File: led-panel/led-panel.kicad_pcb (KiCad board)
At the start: 2 copper layers, 129 parts, among them J1 Conn_01x24

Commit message: routing done
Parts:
- moved J1 2.62 mm to (106.7, 108.0)
- moved D100 1.80 mm to (167.6, 83.8)
- moved D106 1.80 mm to (172.7, 73.7)
- moved D107 1.80 mm to (172.7, 78.7)
- moved D108 1.80 mm to (172.7, 83.8)
- moved D122 1.80 mm to (182.9, 73.7)
- moved D123 1.80 mm to (182.9, 78.7)
- moved D124 1.80 mm to (182.9, 83.8)
- moved D34 1.80 mm to (127.0, 73.7)
- moved D35 1.80 mm to (127.0, 78.7)
- moved D36 1.80 mm to (127.0, 83.8)
- moved D50 1.80 mm to (137.2, 73.7)
- moved D51 1.80 mm to (137.2, 78.7)
- moved D52 1.80 mm to (137.2, 83.8)
- moved D66 1.80 mm to (147.3, 73.7)
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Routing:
- net Net-(D0-Pad2): track 0.00 -> 136.9 mm, vias 0 -> 1
- net Net-(D1-Pad2): track 0.00 -> 131.9 mm, vias 0 -> 1
- net Net-(D10-Pad2): track 0.00 -> 126.8 mm, vias 0 -> 1
- net Net-(D107-Pad2): track 0.00 -> 121.7 mm, vias 0 -> 1
- net Net-(D100-Pad2): track 0.00 -> 116.6 mm, vias 0 -> 1
- net Net-(D101-Pad2): track 0.00 -> 111.6 mm, vias 0 -> 1
- net Net-(D102-Pad2): track 0.00 -> 106.4 mm, vias 0 -> 1
- net Net-(D103-Pad2): track 0.00 -> 100.3 mm
- net Net-(D0-Pad1): track 0.00 -> 60.9 mm
- net Net-(D10-Pad1): track 0.00 -> 58.4 mm
- net Net-(D120-Pad1): track 0.00 -> 57.7 mm
- net Net-(D16-Pad1): track 0.00 -> 55.9 mm
- net Net-(D112-Pad1): track 0.00 -> 55.2 mm
- net Net-(D24-Pad1): track 0.00 -> 53.3 mm
- net Net-(D104-Pad1): track 0.00 -> 52.6 mm
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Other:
- board outline added: 83.8 x 50.8 mm

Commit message: fix the routing
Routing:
- net Net-(D10-Pad2): track 126.8 -> 130.5 mm
- net Net-(D103-Pad2): track 100.3 -> 104.0 mm
- net Net-(D102-Pad2): track 106.4 -> 110.2 mm
- net Net-(D107-Pad2): track 121.7 -> 125.4 mm
- net Net-(D0-Pad2): track 136.9 -> 140.6 mm
- net Net-(D100-Pad2): track 116.6 -> 120.3 mm
- net Net-(D101-Pad2): track 111.6 -> 115.2 mm
- net Net-(D1-Pad2): track 131.9 -> 135.6 mm
- added copper zone on B.Cu, net (none)

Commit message: update header footprint silkscreen
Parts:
- J1: footprint Connector_PinHeader_2.54mm:PinHeader_1x24_P2.54mm_Vertical -> led-panel:PinHeader_1x8+16_P2.54mm_Vertical
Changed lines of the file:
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@@
     (35 F.Paste user)
     (36 B.SilkS user)
-    (37 F.SilkS user hide)
+    (37 F.SilkS user)
     (38 B.Mask user)
     (39 F.Mask user)
@@
     (46 B.CrtYd user)
     (47 F.CrtYd user)
-    (48 B.Fab user)
+    (48 B.Fab user hide)
     (49 F.Fab user hide)
   )
@@
     )
   )
-  (module Connector_PinHeader_2.54mm:PinHeader_1x24_P2.54mm_Vertical (layer F.Cu)
+  (module led-panel:PinHeader_1x8+16_P2.54mm_Vertical (layer F.Cu)
     (at 106.68 107.95 90)
     (descr "Through hole straight pin header, 1x24, 2.54mm pitch, single row")
@@
     (fp_line (start -1.27 -0.635) (end -0.635 -1.27) (layer F.Fab) (width 0.1))
     (fp_line (start -1.33 59.75) (end 1.33 59.75) (layer F.SilkS) (width 0.12))
-    (fp_line (start -1.33 1.27) (end -1.33 59.75) (layer F.SilkS) (width 0.12))
-    (fp_line (start 1.33 1.27) (end 1.33 59.75) (layer F.SilkS) (width 0.12))
-    (fp_line (start -1.33 1.27) (end 1.33 1.27) (layer F.SilkS) (width 0.12))
-    (fp_line (start -1.33 0) (end -1.33 -1.33) (layer F.SilkS) (width 0.12))
-    (fp_line (start -1.33 -1.33) (end 0 -1.33) (layer F.SilkS) (width 0.12))
+    (fp_line (start -1.3335 -1.3335) (end -1.33 59.75) (layer F.SilkS) (width 0.12))
+    (fp_line (start 1.3335 -1.3335) (end 1.33 59.75) (layer F.SilkS) (width 0.12))
+    (fp_line (start -1.3335 -1.3335) (end 1.3335 -1.3335) (layer F.SilkS) (width 0.12))
     (fp_line (start -1.8 -1.8) (end -1.8 60.2) (layer F.CrtYd) (width 0.05))
     (fp_line (start -1.8 60.2) (end 1.8 60.2) (layer F.CrtYd) (width 0.05))
@@
       (effects (font (size 1 1) (thickness 0.15)))
     )
+    (fp_line (start -1.3335 19.05) (end 1.3335 19.05) (layer F.SilkS) (width 0.12))
     (pad 1 thru_hole rect (at 0 0 90) (size 1.7 1.7) (drill 1) (layers *.Cu *.Mask)
       (net 1 "Net-(D0-Pad2)"))

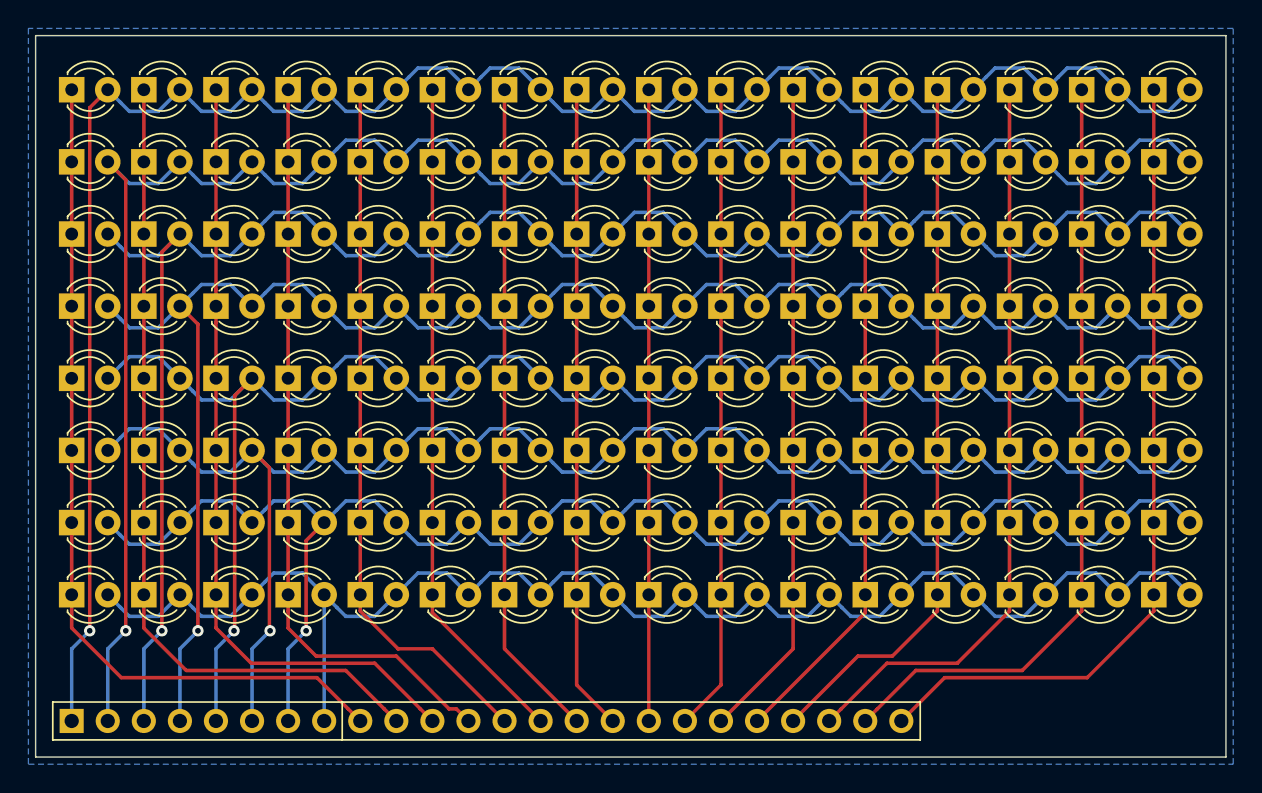
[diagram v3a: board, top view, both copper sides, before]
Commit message: fix led silkscreen
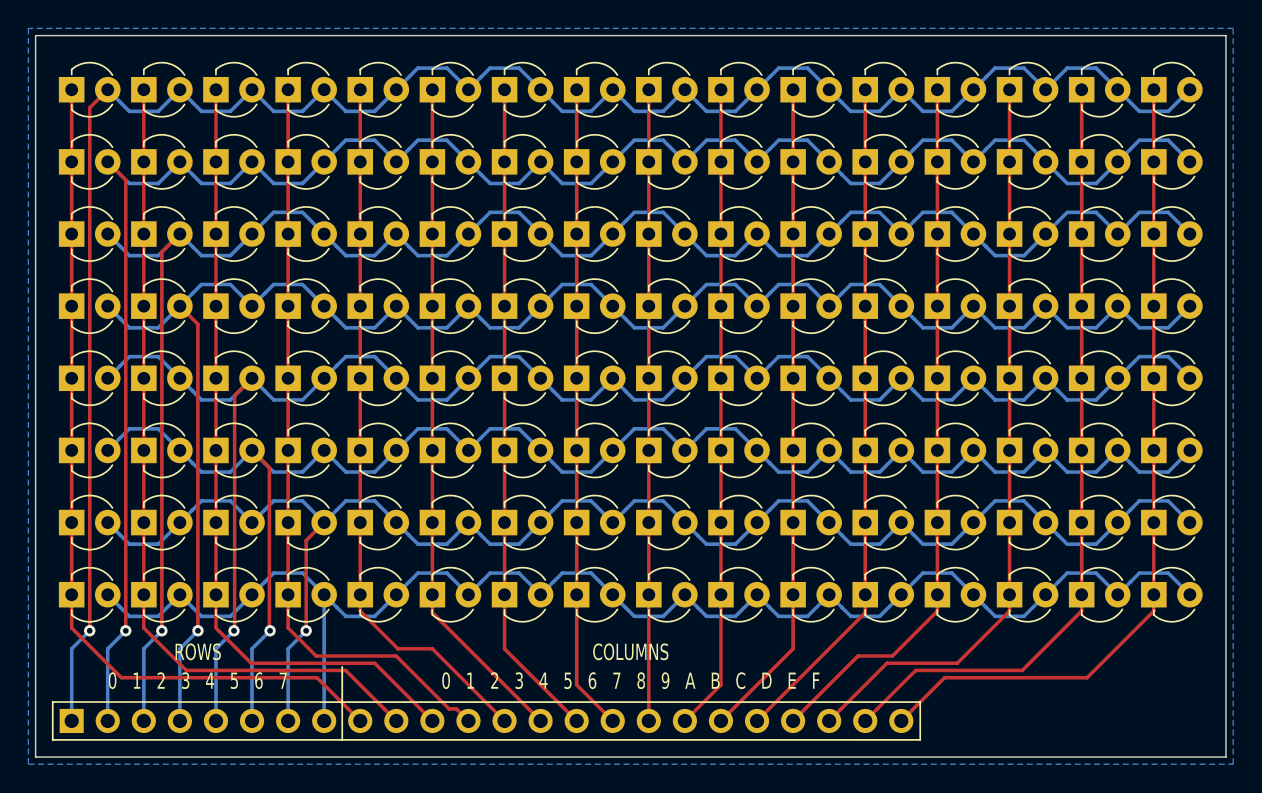
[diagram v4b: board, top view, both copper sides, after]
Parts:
- D0, D1, D10, D100, D101, D102, D103, D104, D105, D106, D107, D108, D109, D11, D110, D111, D112, D113, D114, D115, D116, D117, D118, D119, D12, D120, D121, D122, D123, D124, D125, D126, D127, D13, D14, D15, D16, D17, D18, D19, D2, D20, D21, D22, D23, D24, D25, D26, D27, D28, D29, D3, D30, D31, D32, D33, D34, D35, D36, D37, D38, D39, D4, D40, D41, D42, D43, D44, D45, D46, D47, D48, D49, D5, D50, D51, D52, D53, D54, D55, D56, D57, D58, D59, D6, D60, D61, D62, D63, D64, D65, D66, D67, D68, D69, D7, D70, D71, D72, D73, D74, D75, D76, D77, D78, D79, D8, D80, D81, D82, D83, D84, D85, D86, D87, D88, D89, D9, D90, D91, D92, D93, D94, D95, D96, D97, D98, D99: footprint LED_THT:LED_D3.0mm -> led-panel:LED_D3.0mm
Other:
- board text added: "0 1 2 3 4 5 6 7"
- board text added: "0 1 2 3 4 5 6 7 8 9 A B C D E F"
- board text added: "COLUMNS"
- board text added: "ROWS"
